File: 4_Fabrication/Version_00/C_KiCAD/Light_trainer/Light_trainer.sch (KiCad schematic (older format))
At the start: 69 parts

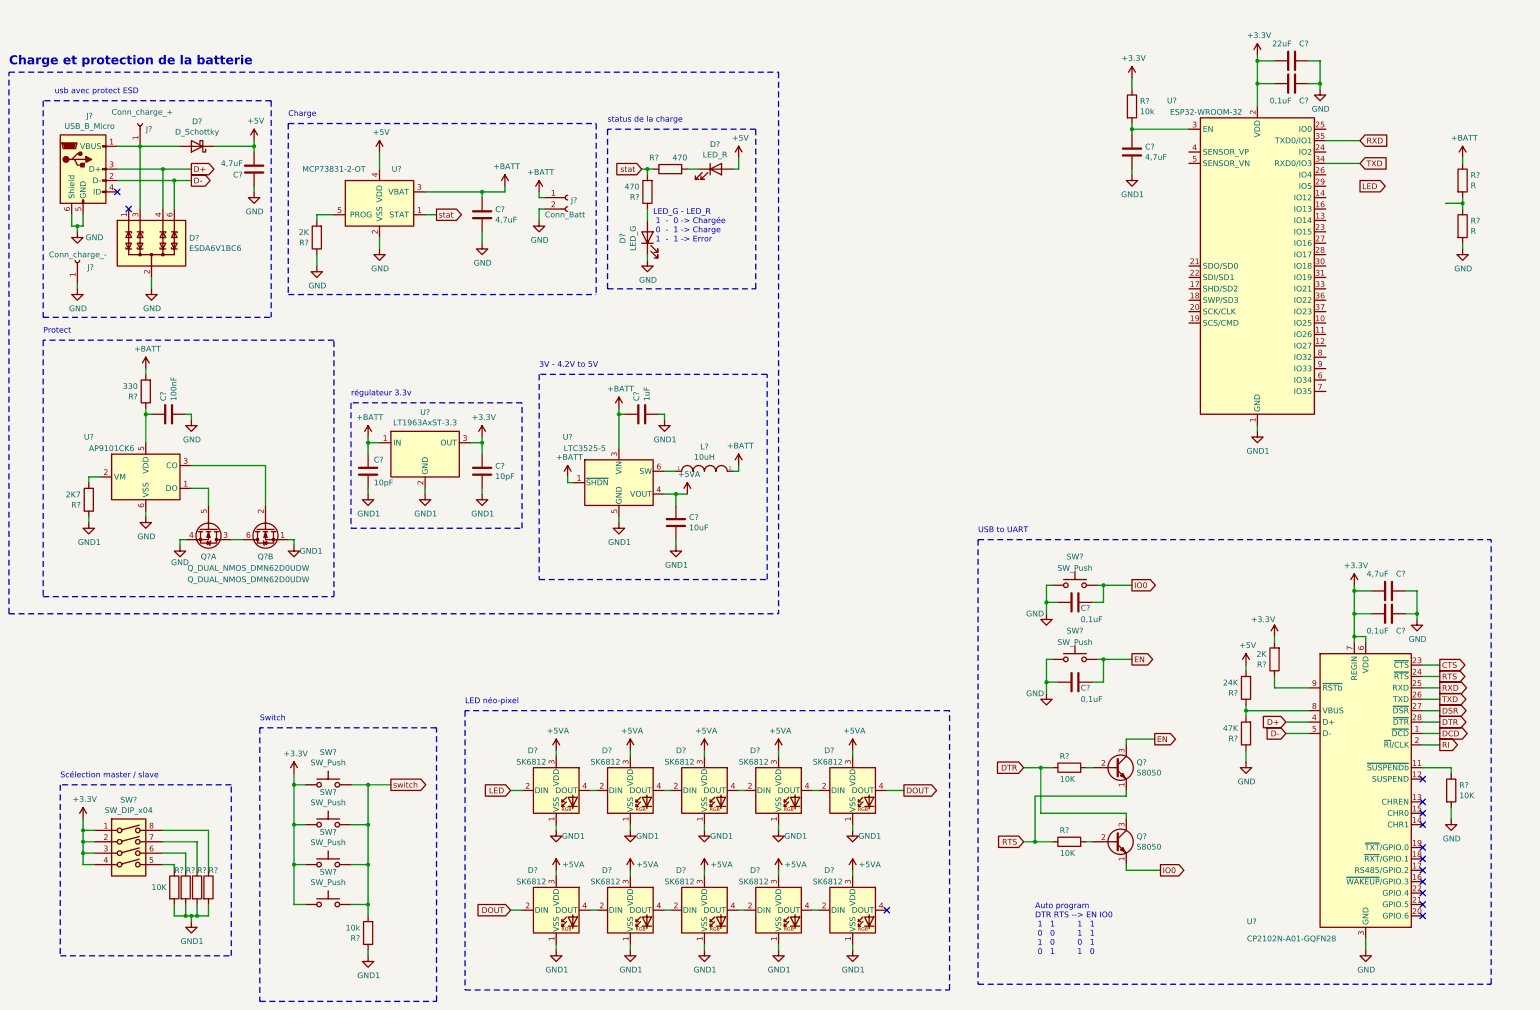
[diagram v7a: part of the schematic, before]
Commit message: modif KiCad
modif protect batt
change usb driver
add data sheet and foot print
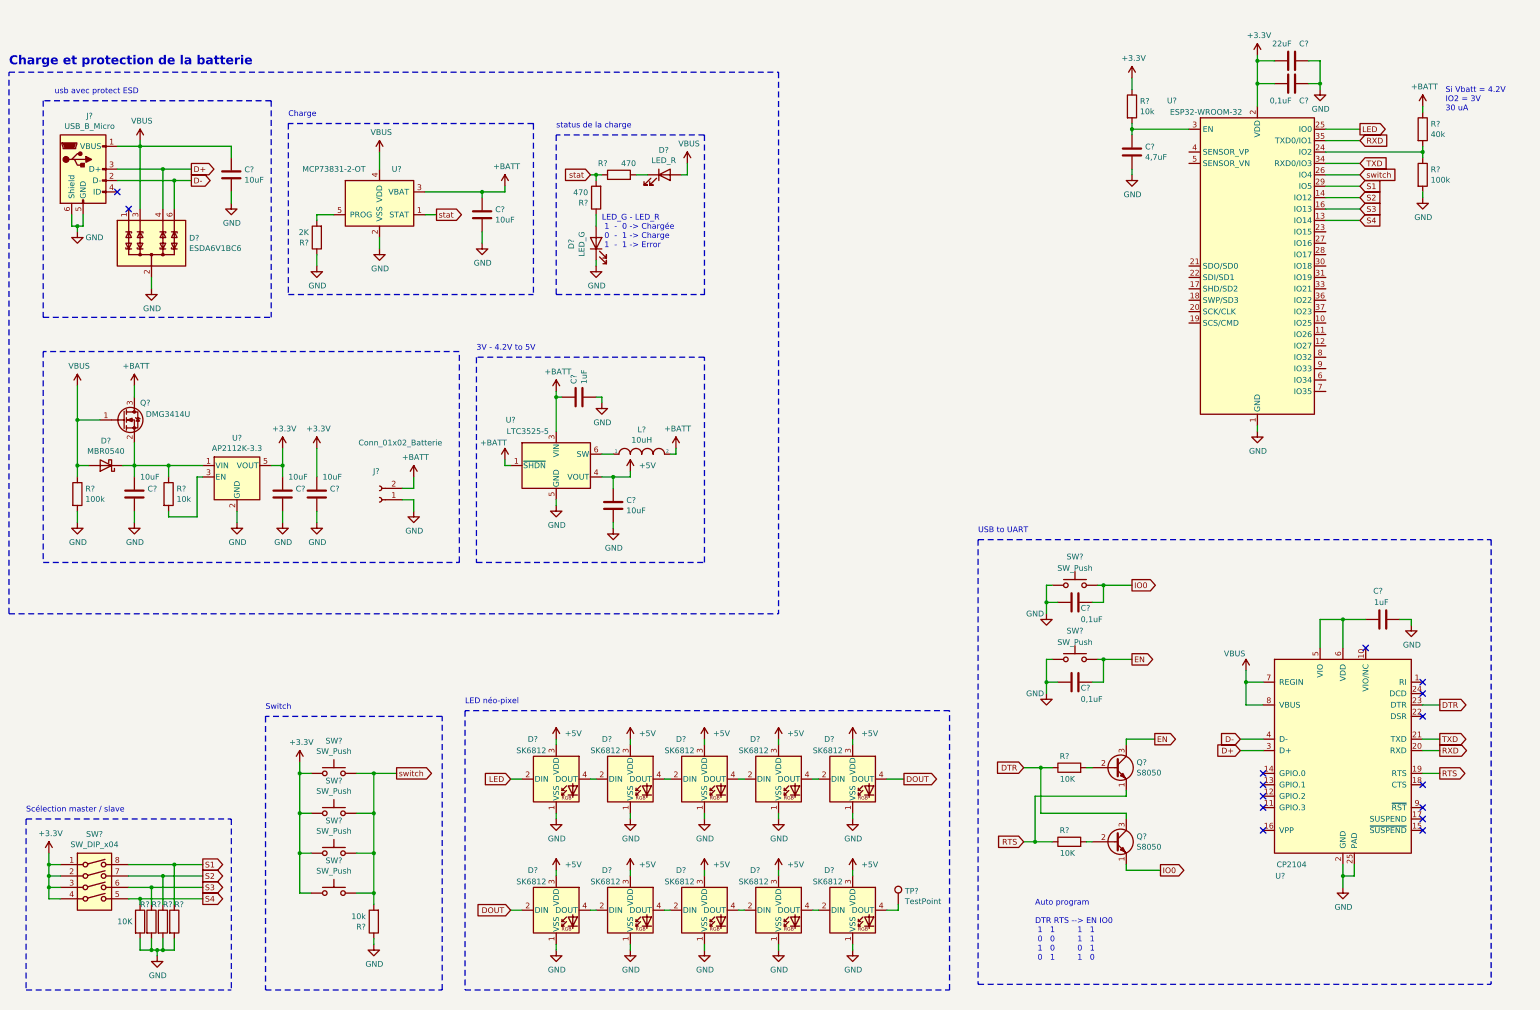
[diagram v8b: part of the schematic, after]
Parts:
- removed C? (x2): 4,7uF, symbol Device:C
- removed C? (x2): 10pF, symbol Device:C
- removed C?: 100nF, symbol Device:C
- removed D?: D_Schottky, symbol Device:D_Schottky
- removed J?: Conn_charge_+, Connector_Wire:SolderWire-0.1sqmm_1x01_D0.4mm_OD1mm, symbol Connector:Conn_01x01_Female
- removed J?: Conn_charge_-, Connector_Wire:SolderWire-0.1sqmm_1x01_D0.4mm_OD1mm, symbol Connector:Conn_01x01_Female
- removed J?: Conn_Batt, Connector_Wire:SolderWire-0.1sqmm_1x02_P3.6mm_D0.4mm_OD1mm_Relief, symbol Connector:Conn_01x02_Female
- removed Q? (x2): Q_DUAL_NMOS_DMN62D0UDW, symbol Light_trainer-rescue:Q_DUAL_NMOS_DMN62D0UDW-Device
- removed R?: 330, Resistor_SMD:R_0805_2012Metric, symbol Device:R
- removed R?: 2K7, Resistor_SMD:R_0805_2012Metric, symbol Device:R
- removed R?: 2K, Resistor_SMD:R_0805_2012Metric, symbol Device:R
- removed R?: 24K, Resistor_SMD:R_0805_2012Metric, symbol Device:R
- removed R?: 47K, Resistor_SMD:R_0805_2012Metric, symbol Device:R
- removed R?: 10K, Resistor_SMD:R_0805_2012Metric, symbol Device:R
- removed U?: LT1963AxST-3.3, Package_TO_SOT_SMD:SOT-223-3_TabPin2, symbol Regulator_Linear:LT1963AxST-3.3
- removed U?: AP9101CK6, Package_TO_SOT_SMD:SOT-23-6, symbol Battery_Management:AP9101CK6
- removed U?: CP2102N-A01-GQFN28, Package_DFN_QFN:QFN-28-1EP_5x5mm_P0.5mm_EP3.35x3.35mm, symbol Interface_USB:CP2102N-A01-GQFN28
- added C? (x4): 10uF, Capacitor_SMD:C_0805_2012Metric, symbol Device:C
- added D?: MBR0540, Diode_SMD:D_SOD-123, symbol Diode:MBR0540
- added J?: Conn_01x02_Batterie, Connector_JST:JST_PH_B2B-PH-K_1x02_P2.00mm_Vertical, symbol Connector:Conn_01x02_Female
- added Q?: DMG3414U, Package_TO_SOT_SMD:SOT-23, symbol Transistor_FET:DMG3414U
- added R?: 10k, Resistor_SMD:R_0805_2012Metric, symbol Device:R
- added R?: 100k, Resistor_SMD:R_0805_2012Metric, symbol Device:R
- added TP?: TestPoint, TestPoint:TestPoint_THTPad_2.5x2.5mm_Drill1.2mm, symbol Connector:TestPoint
- added U?: AP2112K-3.3, Package_TO_SOT_SMD:SOT-23-5, symbol Regulator_Linear:AP2112K-3.3
- added U?: CP2104, Package_DFN_QFN:QFN-24-1EP_4x4mm_P0.5mm_EP2.6x2.6mm, symbol Interface_USB:CP2104
- C?: value 4,7uF -> 10uF; footprint (none) -> Capacitor_SMD:C_0805_2012Metric
- C? (x7): footprint (none) -> Capacitor_SMD:C_0805_2012Metric
- C?: value 0,1uF -> 1uF; footprint (none) -> Capacitor_SMD:C_0805_2012Metric
- D?: footprint (none) -> LED_SMD:LED_1806_4516Metric; Fournisseur (none) -> Digitek; Prix total (none) -> 0,32; prix unité (none) -> 0,32
- D?: footprint (none) -> LED_SMD:LED_1806_4516Metric; Fournisseur (none) -> Digitek; Prix total (none) -> 0,56; prix unité (none) -> 0,56
- Q? (x2), R? (x11): Fournisseur (none) -> Digikey
- R?: value R -> 40k; footprint (none) -> Resistor_SMD:R_0805_2012Metric; Fournisseur (none) -> Digikey
- R?: value R -> 100k; footprint (none) -> Resistor_SMD:R_0805_2012Metric; Fournisseur (none) -> Digikey
- SW? (x6): footprint (none) -> Button_Switch_SMD:SW_SPST_PTS645; Fournisseur (none) -> Digikey; Prix total (none) -> 0,22; prix unité (none) -> 1,32
- SW?: footprint (none) -> Package_DIP:SMDIP-8_W7.62mm; Fournisseur (none) -> Digikey; Prix total (none) -> 0,45; prix unité (none) -> 0,45
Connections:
- net +5VA is gone; now on net +5V: C?.1, D?.3 (VDD), D?.3 (VDD), D?.3 (VDD), D?.3 (VDD), D?.3 (VDD), D?.3 (VDD), D?.3 (VDD), D?.3 (VDD), D?.3 (VDD), D?.3 (VDD), U?.4 (VOUT)
- net GND1 is gone; now on net GND: C?.2, C?.2, C?.2, D?.1 (VSS), D?.1 (VSS), D?.1 (VSS), D?.1 (VSS), D?.1 (VSS), D?.1 (VSS), D?.1 (VSS), D?.1 (VSS), D?.1 (VSS), D?.1 (VSS), R?.1, R?.2, R?.2, R?.2, R?.2, U?.1 (GND), U?.15 (GND), U?.2 (GND), U?.38 (GND), U?.39 (GND), U?.5 (GND)
- net +3V3: now also C?.1, C?.1, U?.5 (VOUT); no longer C?.1
- net +5V: no longer D?.2 (A), U?.4 (VDD)
- net +BATT: now also J?.2 (Pin_2), Q?.3 (D)
- net D+: now also U?.3 (D+)
- net D-: now also U?.4 (D-)
- net DTR: now also U?.23 (DTR)
- net GND: now also C?.2, C?.2, C?.2, C?.2, J?.1 (Pin_1), R?.2, U?.2 (GND), U?.2 (GND), U?.25 (PAD)
- net LED: now also U?.25 (IO0)
- net RTS: now also U?.19 (RTS)
- net RXD: now also U?.20 (RXD)
- net TXD: now also U?.21 (TXD)
- net switch: now also U?.26 (IO4)
- net VBUS: now reaches D?.3 (TVS2), J?.1 (VBUS)
- net VBUS: now also D?.2 (A), U?.4 (VDD), C?.1, D?.2 (A), Q?.1 (G), R?.1, U?.7 (REGIN), U?.8 (VBUS)
- net S4: now reaches U?.13 (IO14)
- net S4: now also R?.1, SW?.5
- net S2: now reaches U?.14 (IO12)
- net S2: now also R?.1, SW?.7
- net S3: now reaches U?.16 (IO13)
- net S3: now also R?.1, SW?.6
- net at U?.24 (IO2): now also R?.1, R?.2
- net S1: now reaches U?.29 (IO5)
- net S1: now also R?.1, SW?.8
- net at D?.4 (DOUT): now also TP?.1
- new net: C?.1, U?.5 (VIO), U?.6 (VDD)
- new net: C?.1, D?.1 (K), Q?.2 (S), R?.1, U?.1 (VIN)
- new net: R?.2, U?.3 (EN)
- no-connect marks 14 -> 15
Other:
- note added: "Auto program\n\nDTR RTS --> EN IO0\n 1 1 1 1\n 0 0 1 1\n 1 0 0 1\n 0 1 1 0"
- note added: "Si Vbatt = 4.2V \nIO2 = 3V\n30 uA"
- note removed: "Auto program\nDTR RTS --> EN IO0\n 1 1 1 1\n 0 0 1 1\n 1 0 0 1\n 0 1 1 0"
- note removed: "Protect"
- note removed: "régulateur 3.3v"
- moved on the sheet: C?, D?, L?, R?, SW?, U?
